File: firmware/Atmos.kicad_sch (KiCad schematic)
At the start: 69 parts, among them J1 AS3935 breakout, J2 BME280 breakout, J3 USB_C_Receptacle_USB2.0_16P, J4 Micro_SD_Card, J5 Solar power input, J6 Conn_Coaxial, Q1 PMOS_Substrate, Q2 PMOS_Substrate, Q3 PMOS_Substrate, SW2 SW_Push, U1 ESP32-S3-WROOM-1, U10 TPS22918DBVR, U11 MAX17048G_T10, U12 CN3791, U13 SGP40-D-R4, U2 AP2112K-3.3, U3 DS3231M, U4 PMS5003, U5 LTC4412xS6, U7 RFM95W-915S2, U8 USBLC6-2SC6, U9 TPS61023DRLR

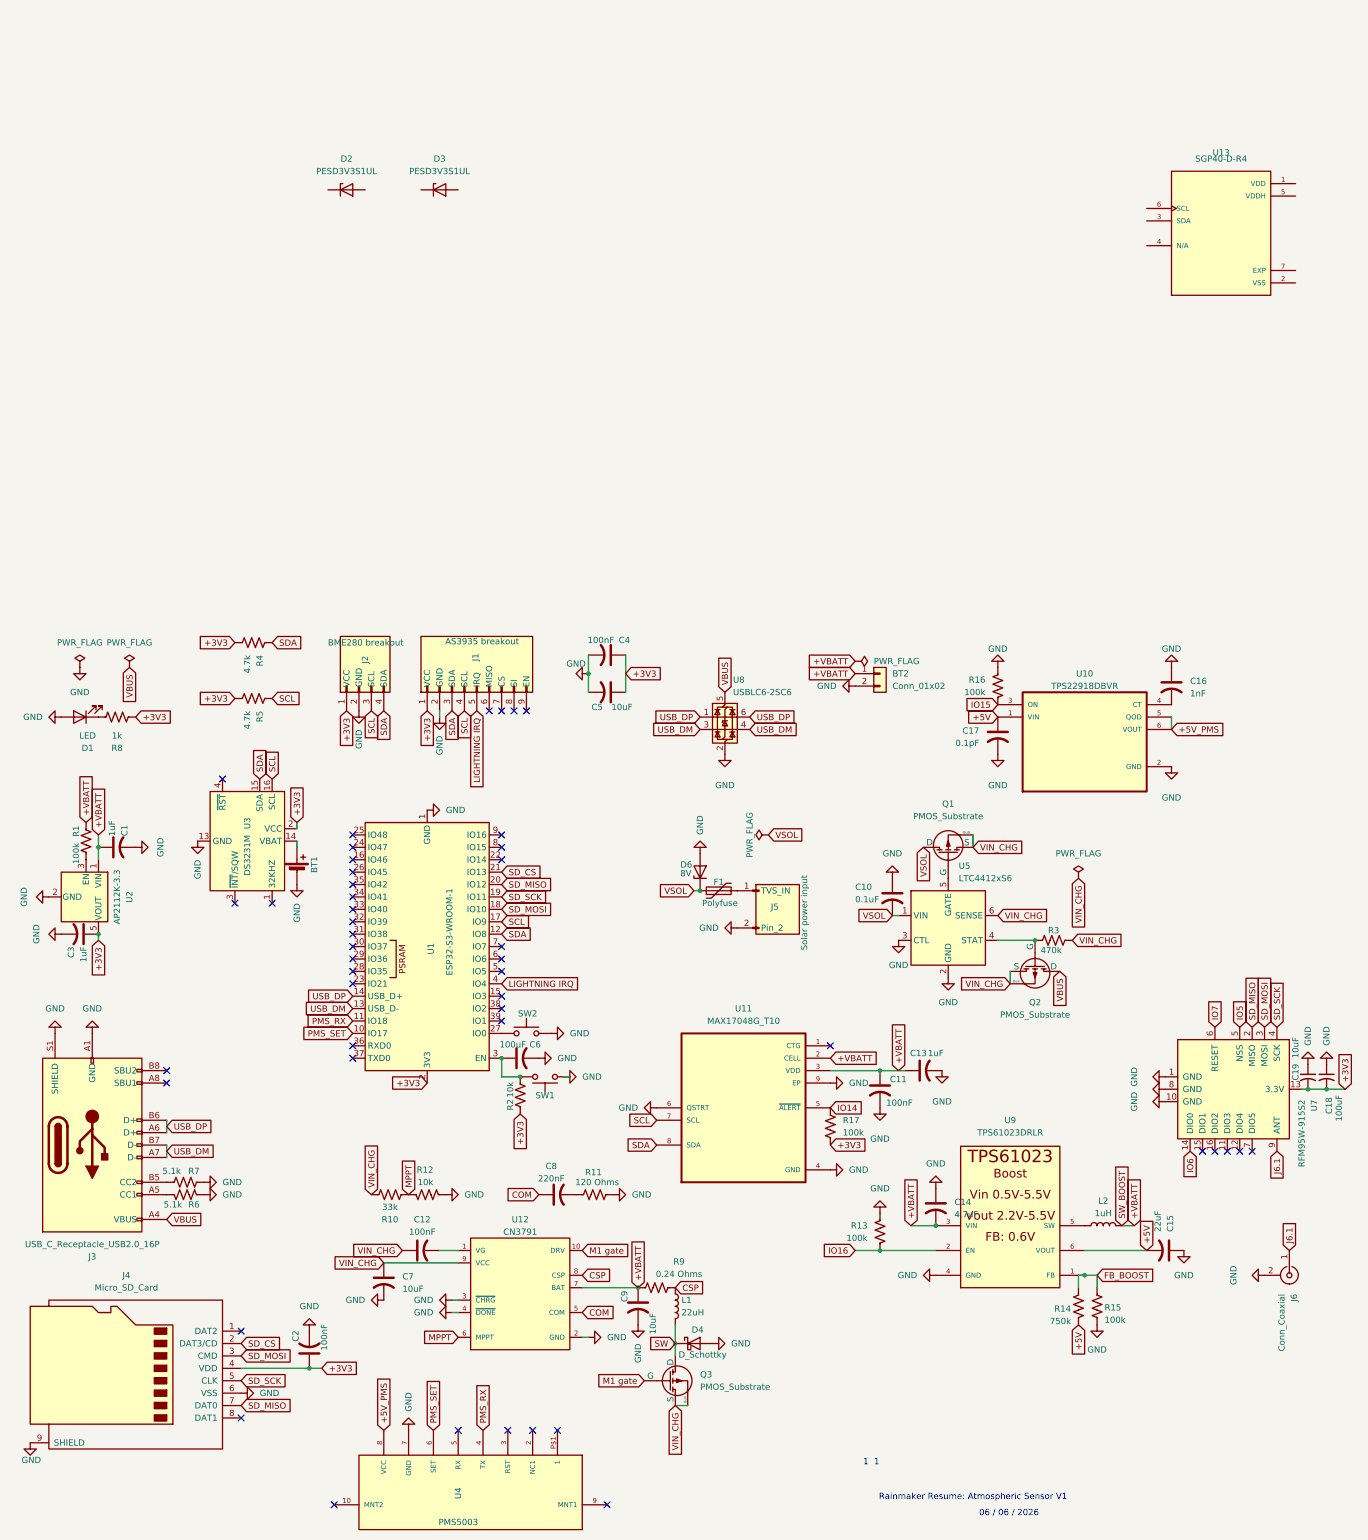
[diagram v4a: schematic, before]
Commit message: added diodes
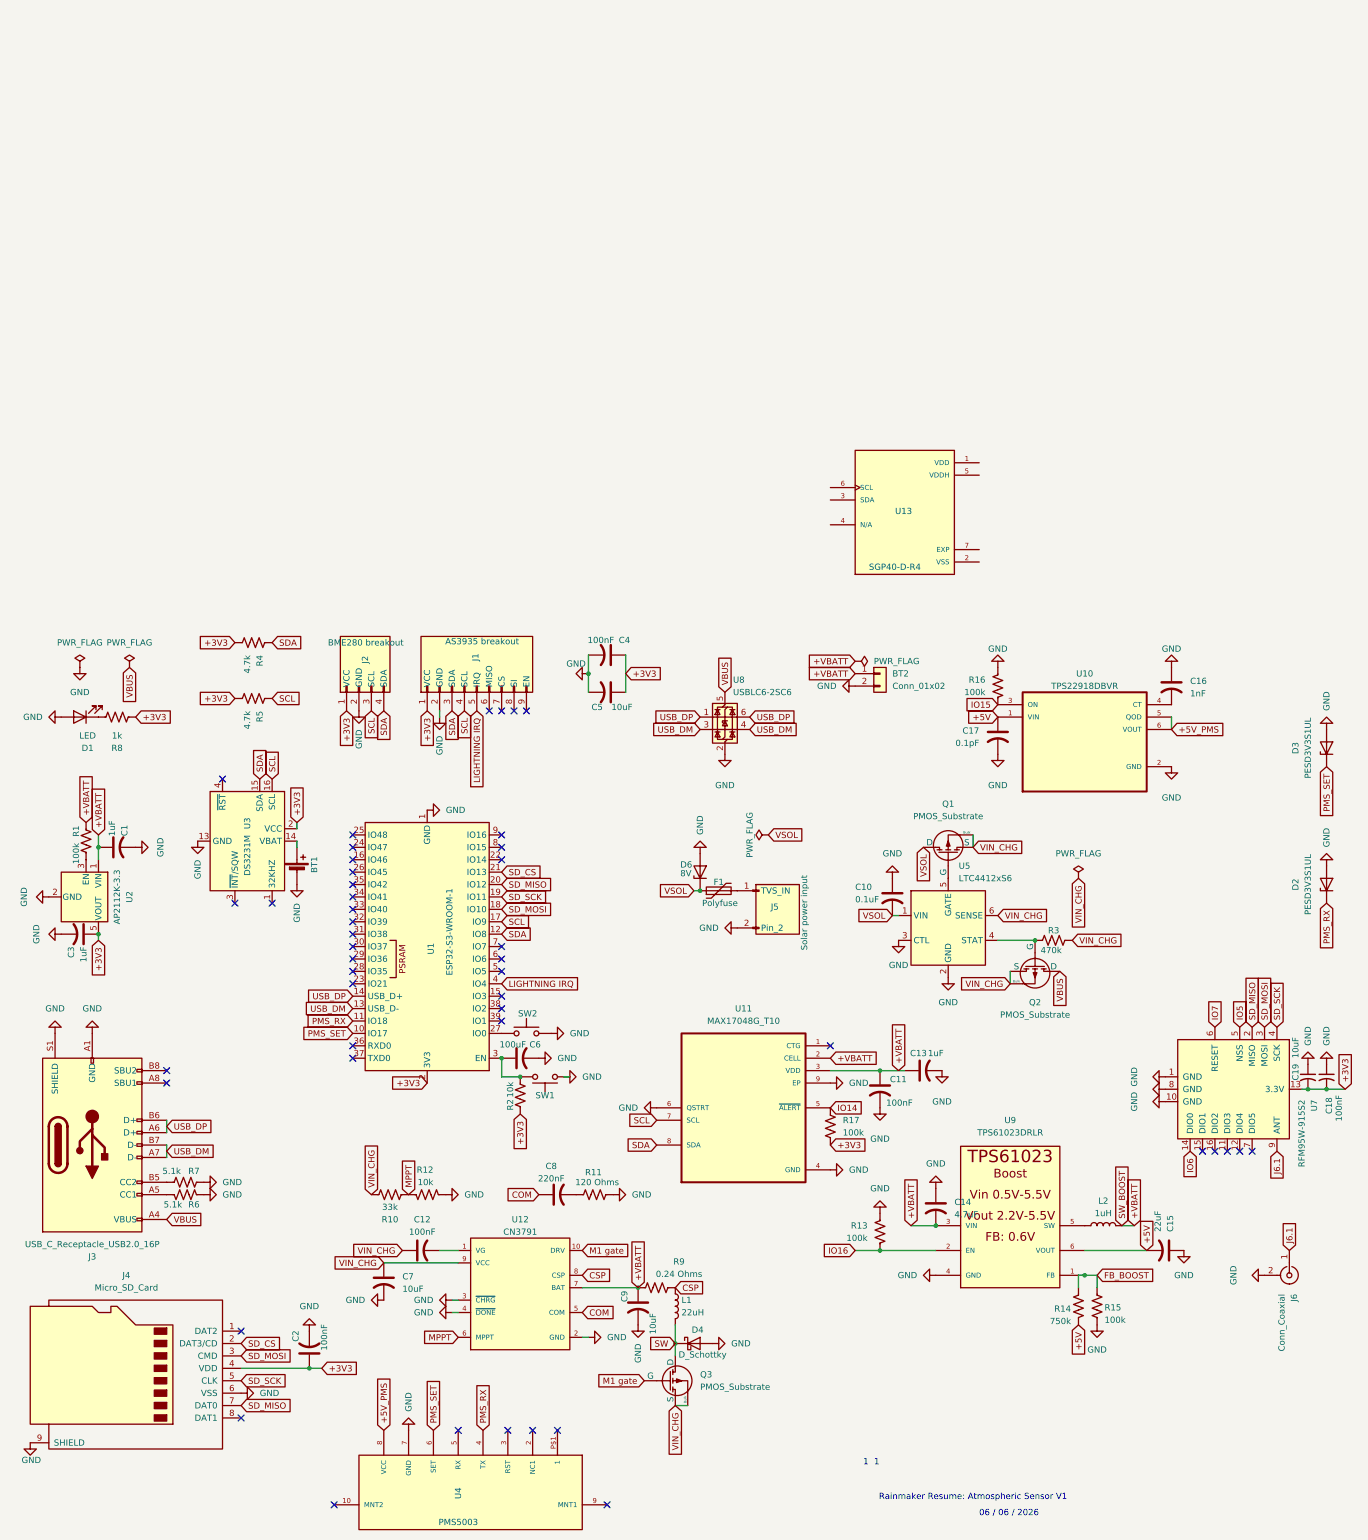
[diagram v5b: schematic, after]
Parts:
- C18: value 100uF -> 100nF
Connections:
- net GND: now also D2.2 (A), D3.2 (A)
- net PMS_RX: now also D2.1 (K)
- net PMS_SET: now also D3.1 (K)
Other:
- moved on the sheet: D2, D3, U13
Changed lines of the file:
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@@
 		)
 	)
+	(global_label "PMS_SET"
+		(shape input)
+		(at 280.67 40.64 270)
+		(fields_autoplaced yes)
+		(effects
+			(font
+				(size 1.27 1.27)
+			)
+			(justify right)
+		)
+		(property "Intersheetrefs" "${INTERSHEET_REFS}"
+			(at 280.67 51.8498 90)
+			(effects
+				(font
+					(size 1.27 1.27)
+				)
+				(justify right)
+				(hide yes)
+			)
+		)
+	)
 	(global_label "LIGHTNING IRQ"
 		(shape input)
@@
 		)
 	)
+	(global_label "PMS_RX"
+		(shape input)
+		(at 280.67 68.58 270)
+		(fields_autoplaced yes)
+		(effects
+			(font
+				(size 1.27 1.27)
+			)
+			(justify right)
+		)
+		(property "Intersheetrefs" "${INTERSHEET_REFS}"
+			(at 280.67 78.9432 90)
+			(effects
+				(font
+					(size 1.27 1.27)
+				)
+				(justify right)
+				(hide yes)
+			)
+		)
+	)
 	(global_label "USB_DP"
 		(shape input)
@@
 	(symbol
 		(lib_id "power:GND")
+		(at 280.67 60.96 180)
+		(unit 1)
+		(exclude_from_sim no)
+		(in_bom yes)
+		(on_board yes)
+		(dnp no)
+		(fields_autoplaced yes)
+		(property "Reference" "#PWR058"
+			(at 280.67 54.61 0)
+			(effects
+				(font
+					(size 1.27 1.27)
+				)
+				(hide yes)
+			)
+		)
+		(property "Value" "GND"
+			(at 280.6699 57.15 90)
+			(effects
+				(font
+					(size 1.27 1.27)
+				)
+				(justify right)
+			)
+		)
+		(property "Footprint" ""
+			(at 280.67 60.96 0)
+			(effects
+				(font
+					(size 1.27 1.27)
+				)
+				(hide yes)
+			)
+		)
+		(property "Datasheet" ""
+			(at 280.67 60.96 0)
+			(effects
+				(font
+					(size 1.27 1.27)
+				)
+				(hide yes)
+			)
+		)
+		(property "Description" "Power symbol creates a global label with name \"GND\" , ground"
+			(at 280.67 60.96 0)
+			(effects
+				(font
+					(size 1.27 1.27)
+				)
+				(hide yes)
+			)
+		)
+		(pin "1"
+		)
+		(instances
+			(project ""
+				(path "/821c823f-0cdf-48e4-87e1-02b442913dca"
+					(reference "#PWR058")
+					(unit 1)
+				)
+			)
+		)
+	)
+	(symbol
+		(lib_id "power:GND")
 		(at 15.24 179.07 0)
 		(mirror y)
@@
 	(symbol
 		(lib_id "SGP40-D-R4:SGP40-D-R4")
-		(at 259.08 -68.58 0)
+		(at 194.31 -11.43 0)
 		(unit 1)
 		(exclude_from_sim no)
@@
 		(on_board yes)
 		(dnp no)
-		(fields_autoplaced yes)
 		(property "Reference" "U13"
-			(at 259.08 -85.09 0)
+			(at 194.056 -11.684 0)
 			(effects
 				(font
@@
 		)
 		(property "Value" "SGP40-D-R4"
-			(at 259.08 -83.82 0)
+			(at 192.278 -0.254 0)
 			(effects
 				(font
@@
 		)
 		(property "Footprint" "SGP40-D-R4:XCDR_SGP40-D-R4"
-			(at 259.08 -68.58 0)
+			(at 194.31 -11.43 0)
 			(effects
 				(font
@@
 		)
 		(property "Datasheet" ""
-			(at 259.08 -68.58 0)
+			(at 194.31 -11.43 0)
 			(effects
 				(font
@@
 		)
 		(property "Description" ""
-			(at 259.08 -68.58 0)
+			(at 194.31 -11.43 0)
 			(effects
 				(font
@@
 		)
 		(property "MF" "Sensirion AG"
-			(at 259.08 -68.58 0)
+			(at 194.31 -11.43 0)
 			(effects
 				(font
@@
 		)
 		(property "MAXIMUM_PACKAGE_HEIGHT" "0.95mm"
-			(at 259.08 -68.58 0)
+			(at 194.31 -11.43 0)
 			(effects
 				(font
@@
 		)
 		(property "Package" "None"
-			(at 259.08 -68.58 0)
+			(at 194.31 -11.43 0)
 			(effects
 				(font
@@
 		)
 		(property "Price" "None"
-			(at 259.08 -68.58 0)
+			(at 194.31 -11.43 0)
 			(effects
 				(font
@@
 		)
 		(property "Check_prices" "https://www.snapeda.com/parts/SGP40-D-R4/Sensirion/view-part/?ref=eda"
-			(at 259.08 -68.58 0)
+			(at 194.31 -11.43 0)
 			(effects
 				(font
@@
 		)
 		(property "STANDARD" "Manufacturer Recommendations"
-			(at 259.08 -68.58 0)
+			(at 194.31 -11.43 0)
 			(effects
 				(font
@@
 		)
 		(property "PARTREV" "1.2"
-			(at 259.08 -68.58 0)
+			(at 194.31 -11.43 0)
 			(effects
 				(font
@@
 		)
 		(property "SnapEDA_Link" "https://www.snapeda.com/parts/SGP40-D-R4/Sensirion/view-part/?ref=snap"
-			(at 259.08 -68.58 0)
+			(at 194.31 -11.43 0)
 			(effects
 				(font
@@
 		)
 		(property "MP" "SGP40-D-R4"
-			(at 259.08 -68.58 0)
+			(at 194.31 -11.43 0)
 			(effects
 				(font
@@
 		)
 		(property "Purchase-URL" "https://www.snapeda.com/api/url_track_click_mouser/?unipart_id=5003465&manufacturer=Sensirion AG&part_name=SGP40-D-R4&search_term=None"
-			(at 259.08 -68.58 0)
+			(at 194.31 -11.43 0)
 			(effects
 				(font
@@
 		)
 		(property "Description_1" "AIR QUALITY GAS SENSOR LOW POWER"
-			(at 259.08 -68.58 0)
+			(at 194.31 -11.43 0)
 			(effects
 				(font
@@
 		)
 		(property "MANUFACTURER" "Sensirion AG"
-			(at 259.08 -68.58 0)
+			(at 194.31 -11.43 0)
 			(effects
 				(font
@@
 		)
 		(property "Availability" "In Stock"
-			(at 259.08 -68.58 0)
+			(at 194.31 -11.43 0)
 			(effects
 				(font
@@
 		)
 		(property "SNAPEDA_PN" "SGP40-D-R4"
-			(at 259.08 -68.58 0)
+			(at 194.31 -11.43 0)
 			(effects
 				(font
@@
 	(symbol
 		(lib_id "Diode:PESD3V3S1UL")
-		(at 80.01 -77.47 0)
+		(at 280.67 64.77 90)
 		(unit 1)
 		(exclude_from_sim no)
@@
 		(fields_autoplaced yes)
 		(property "Reference" "D2"
-			(at 80.01 -83.82 0)
+			(at 274.32 64.77 0)
 			(effects
 				(font
@@
 		)
 		(property "Value" "PESD3V3S1UL"
-			(at 80.01 -81.28 0)
+			(at 276.86 64.77 0)
 			(effects
 				(font
@@
 		)
 		(property "Footprint" "Diode_SMD:D_SOD-882"
-			(at 80.01 -72.39 0)
+			(at 285.75 64.77 0)
 			(effects
 				(font
@@
 		)
 		(property "Datasheet" "https://assets.nexperia.com/documents/data-sheet/PESD3V3S1UL.pdf"
-			(at 80.01 -82.55 0)
+			(at 275.59 64.77 0)
 			(effects
 				(font
@@
 		)
 		(property "Description" "Unidirectional ESD protection diode, 3.3V, SOD-882"
-			(at 80.01 -85.09 0)
+			(at 273.05 64.77 0)
 			(effects
 				(font
@@
 	)
 	(symbol
+		(lib_id "power:GND")
+		(at 280.67 33.02 180)
+		(unit 1)
+		(exclude_from_sim no)
+		(in_bom yes)
+		(on_board yes)
+		(dnp no)
+		(fields_autoplaced yes)
+		(property "Reference" "#PWR059"
+			(at 280.67 26.67 0)
+			(effects
+				(font
+					(size 1.27 1.27)
+				)
+				(hide yes)
+			)
+		)
+		(property "Value" "GND"
+			(at 280.6699 29.21 90)
+			(effects
+				(font
+					(size 1.27 1.27)
+				)
+				(justify right)
+			)
+		)
+		(property "Footprint" ""
+			(at 280.67 33.02 0)
+			(effects
+				(font
+					(size 1.27 1.27)
+				)
+				(hide yes)
+			)
+		)
+		(property "Datasheet" ""
+			(at 280.67 33.02 0)
+			(effects
+				(font
+					(size 1.27 1.27)
+				)
+				(hide yes)
+			)
+		)
+		(property "Description" "Power symbol creates a global label with name \"GND\" , ground"
+			(at 280.67 33.02 0)
+			(effects
+				(font
+					(size 1.27 1.27)
+				)
+				(hide yes)
+			)
+		)
+		(pin "1"
+		)
+		(instances
+			(project "Atmos"
+				(path "/821c823f-0cdf-48e4-87e1-02b442913dca"
+					(reference "#PWR059")
+					(unit 1)
+				)
+			)
+		)
+	)
+	(symbol
 		(lib_id "Device:C_US")
 		(at 115.57 100.33 90)
@@
 	(symbol
 		(lib_id "Diode:PESD3V3S1UL")
-		(at 99.06 -77.47 0)
+		(at 280.67 36.83 90)
 		(unit 1)
 		(exclude_from_sim no)
@@
 		(fields_autoplaced yes)
 		(property "Reference" "D3"
-			(at 99.06 -83.82 0)
+			(at 274.32 36.83 0)
 			(effects
 				(font
@@
 		)
 		(property "Value" "PESD3V3S1UL"
-			(at 99.06 -81.28 0)
+			(at 276.86 36.83 0)
 			(effects
 				(font
@@
 		)
 		(property "Footprint" "Diode_SMD:D_SOD-882"
-			(at 99.06 -72.39 0)
+			(at 285.75 36.83 0)
 			(effects
 				(font
@@
 		)
 		(property "Datasheet" "https://assets.nexperia.com/documents/data-sheet/PESD3V3S1UL.pdf"
-			(at 99.06 -82.55 0)
+			(at 275.59 36.83 0)
 			(effects
 				(font
@@
 		)
 		(property "Description" "Unidirectional ESD protection diode, 3.3V, SOD-882"
-			(at 99.06 -85.09 0)
+			(at 273.05 36.83 0)
 			(effects
 				(font
@@
 			)
 		)
-		(property "Value" "100uF"
+		(property "Value" "100nF"
 			(at 283.21 113.284 90)
 			(effects

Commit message: Schematic tentatively finished
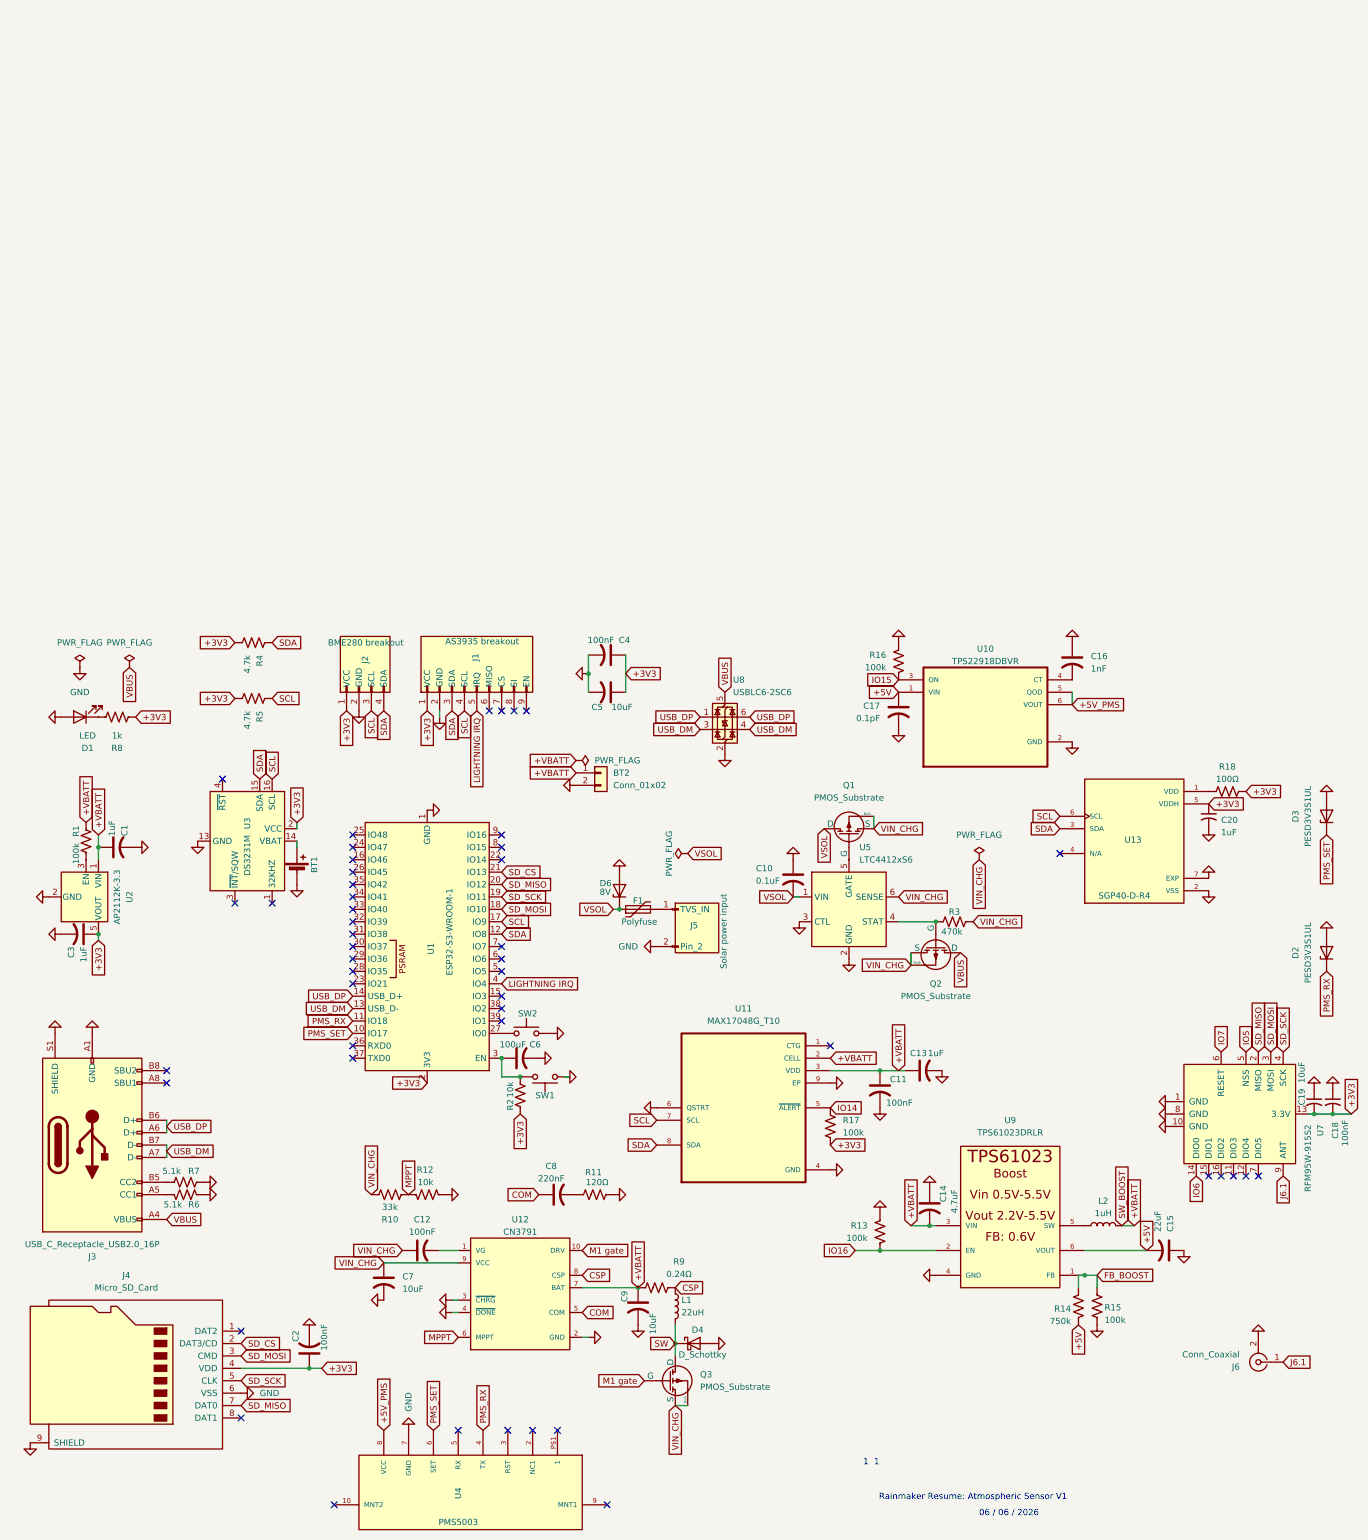
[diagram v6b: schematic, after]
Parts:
- added C20: 1uF, symbol Device:C_Small_US
- added R18: 100Ω, symbol Device:R_US
- R11: value 120 Ohms -> 120Ω
- R9: value 0.24 Ohms -> 0.24Ω
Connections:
- net +3V3: now also U13.5 (VDDH), C20.1, R18.2
- net GND: now also U13.2 (VSS), U13.7 (EXP), C20.2
- net SCL: now also U13.6 (SCL)
- net SDA: now also U13.3 (SDA)
- net at U13.1 (VDD): now also R18.1
- no-connect marks 47 -> 48
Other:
- moved on the sheet: BT2, C10, C14, C16, C17, C18, C19, D2, D3, D6, F1, J5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
